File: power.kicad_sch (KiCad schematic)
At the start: 49 parts, among them J1 Battery 1, J7 Battery 2, J8 USB, U1 AMS1117-3.3, U5 TPS56A37RPAR, U6 TPS56A37RPAR

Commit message: Update Cout models for servo motor power and extended pground
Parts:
- C15, C16: footprint Capacitor_SMD:C_0805_2012Metric -> Capacitor_SMD:C_1210_3225Metric
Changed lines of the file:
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@@
 			)
 		)
-		(property "Footprint" "Capacitor_SMD:C_0805_2012Metric"
+		(property "Footprint" "Capacitor_SMD:C_1210_3225Metric"
 			(at 202.8952 40.64 0)
 			(effects
@@
 			)
 		)
-		(property "Datasheet" "~"
+		(property "Datasheet" "HRE CGA1210X6S106K350QT"
 			(at 201.93 36.83 0)
 			(effects
@@
 			)
 		)
-		(property "Footprint" "Capacitor_SMD:C_0805_2012Metric"
+		(property "Footprint" "Capacitor_SMD:C_1210_3225Metric"
 			(at 213.0552 40.64 0)
 			(effects
@@
 			)
 		)
-		(property "Datasheet" "~"
+		(property "Datasheet" "HRE CGA1210X6S106K350QT"
 			(at 212.09 36.83 0)
 			(effects

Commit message: update inductor
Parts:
- L1: footprint Inductor_SMD:L_0805_2012Metric_Pad1.05x1.20mm_HandSolder -> 74438357033:WE-MAPI_4030
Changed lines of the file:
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@@
 			)
 		)
-		(property "Footprint" "Inductor_SMD:L_0805_2012Metric_Pad1.05x1.20mm_HandSolder"
+		(property "Footprint" "74438357033:WE-MAPI_4030"
 			(at 184.15 31.75 0)
 			(effects
@@
 			)
 		)
-		(property "Datasheet" "~"
+		(property "Datasheet" "FTC404030S3R3MGCA"
 			(at 184.15 31.75 0)
 			(effects

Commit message: Sync
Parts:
- removed C18, C19, C38, C39: 10uF, Capacitor_SMD:C_0805_2012Metric, symbol Device:C
- removed C32, C36: 0.1uF, Capacitor_SMD:C_0805_2012Metric, symbol Device:C
- removed C33: 47nF, Capacitor_SMD:C_0805_2012Metric, symbol Device:C
- removed C37: 150pF, Capacitor_SMD:C_0805_2012Metric, symbol Device:C
- removed D4: B540C-13-F, B540C_13_F:DIOM6959X245N, symbol B540C-13-F:B540C-13-F
- removed D7: RED, LED_SMD:LED_0805_2012Metric, symbol Device:LED
- removed F2: C1F-5, C1F_5:FUSC3215X83N, symbol C1F-5:C1F-5
- removed J7: Battery 2, 39-28-1023:CONN_SD-5566-002_02_MOL, symbol 39-28-1023:39281023
- removed L2: 3.3uH, Inductor_SMD:L_0805_2012Metric_Pad1.05x1.20mm_HandSolder, symbol Device:L_Ferrite
- removed R12: 1k5, Resistor_SMD:R_0805_2012Metric_Pad1.20x1.40mm_HandSolder, symbol Device:R
- removed R21: 169kR, Capacitor_SMD:C_0805_2012Metric, symbol Device:R
- removed R22: 36.1kR, Capacitor_SMD:C_0805_2012Metric, symbol Device:R
- removed R23: 52.3kR, Capacitor_SMD:C_0805_2012Metric, symbol Device:R
- removed R24: 10kR, Capacitor_SMD:C_0805_2012Metric, symbol Device:R
- removed R30: 49.9R, Capacitor_SMD:C_0805_2012Metric, symbol Device:R
- removed R31: 73.2kR, Capacitor_SMD:C_0805_2012Metric, symbol Device:R
- removed U6: TPS56A37RPAR, RPA0010A-MFG, symbol TPS56A37RPAR:TPS56A37RPAR
- added C29, C30: 10uF, Capacitor_SMD:C_1206_3216Metric, symbol Device:C
- added C31, C35: 0.1uF, Capacitor_SMD:C_0805_2012Metric, symbol Device:C
- added C34: 47nF, Capacitor_SMD:C_0805_2012Metric, symbol Device:C
- added C40: 150pF, Capacitor_SMD:C_0805_2012Metric, symbol Device:C
- added C41, C42: 10uF, Capacitor_SMD:C_1210_3225Metric, symbol Device:C
- added D6: B540C-13-F, B540C_13_F:DIOM6959X245N, symbol B540C-13-F:B540C-13-F
- added D8: RED, LED_SMD:LED_0805_2012Metric, symbol Device:LED
- added F3: C1F-5, C1F_5:FUSC3215X83N, symbol C1F-5:C1F-5
- added J3: Battery 1, 1724480002:MOLEX_1724480002, symbol 39-28-1023:39281023
- added L3: 3.3uH, 74438357033:WE-MAPI_4030, symbol Device:L_Ferrite
- added R36: 169kR, Capacitor_SMD:C_0805_2012Metric, symbol Device:R
- added R37: 36.1kR, Capacitor_SMD:C_0805_2012Metric, symbol Device:R
- added R38: 52.3kR, Capacitor_SMD:C_0805_2012Metric, symbol Device:R
- added R39: 10kR, Capacitor_SMD:C_0805_2012Metric, symbol Device:R
- added R40: 49.9R, Capacitor_SMD:C_0805_2012Metric, symbol Device:R
- added R41: 73.2kR, Capacitor_SMD:C_0805_2012Metric, symbol Device:R
- added R42: 1k5, Capacitor_SMD:C_0805_2012Metric, symbol Device:R
- added U8: TPS56A37RPAR, RPA0010A-MFG, symbol TPS56A37RPAR:TPS56A37RPAR
- J1: footprint 39-28-1023:CONN_SD-5566-002_02_MOL -> 1724480002:MOLEX_1724480002
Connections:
- net 5V_CAM: now also C41.1, C42.1, L3.2, R40.1, R42.1
- net BT_CAM: now also C35.1, U8.7 (BOOT)
- net EN_CAM_PWR: now also R36.2, R37.1, U8.1 (EN)
- net FB_CAM_PWR: now also C40.2, R39.1, R41.2, U8.2 (FB)
- net GND: now also C29.2, C30.2, C31.2, C34.2, C41.2, C42.2, D8.1 (K), J3.2, R37.2, R38.1, R39.2, U8.3 (AGND), U8.9 (PGND)
- net MODE_CAM: now also R38.2, U8.10 (MODE)
- net SS_CAM: now also C34.1, U8.5 (SS)
- net SW_CAM_PWR: now also C35.2, L3.1, U8.6 (SW)
- net VIN_CAM: now also C29.1, C30.1, C31.1, D6.C, R36.1, U8.8 (VIN)
- new net: C40.1, R40.2, R41.1
- new net: F3.1, J3.1
- new net: D8.2 (A), R42.2
- new net BAT_2: D6.A, F3.2
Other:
- note added: "LED Indicate Battery Supply to Camera"
- note removed: "LED Indicate Battery Supply to Cameras"
- moved on the sheet: C10, C11, C12, C13, C14, C15, C16, C17, C7, C8, D1, D2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

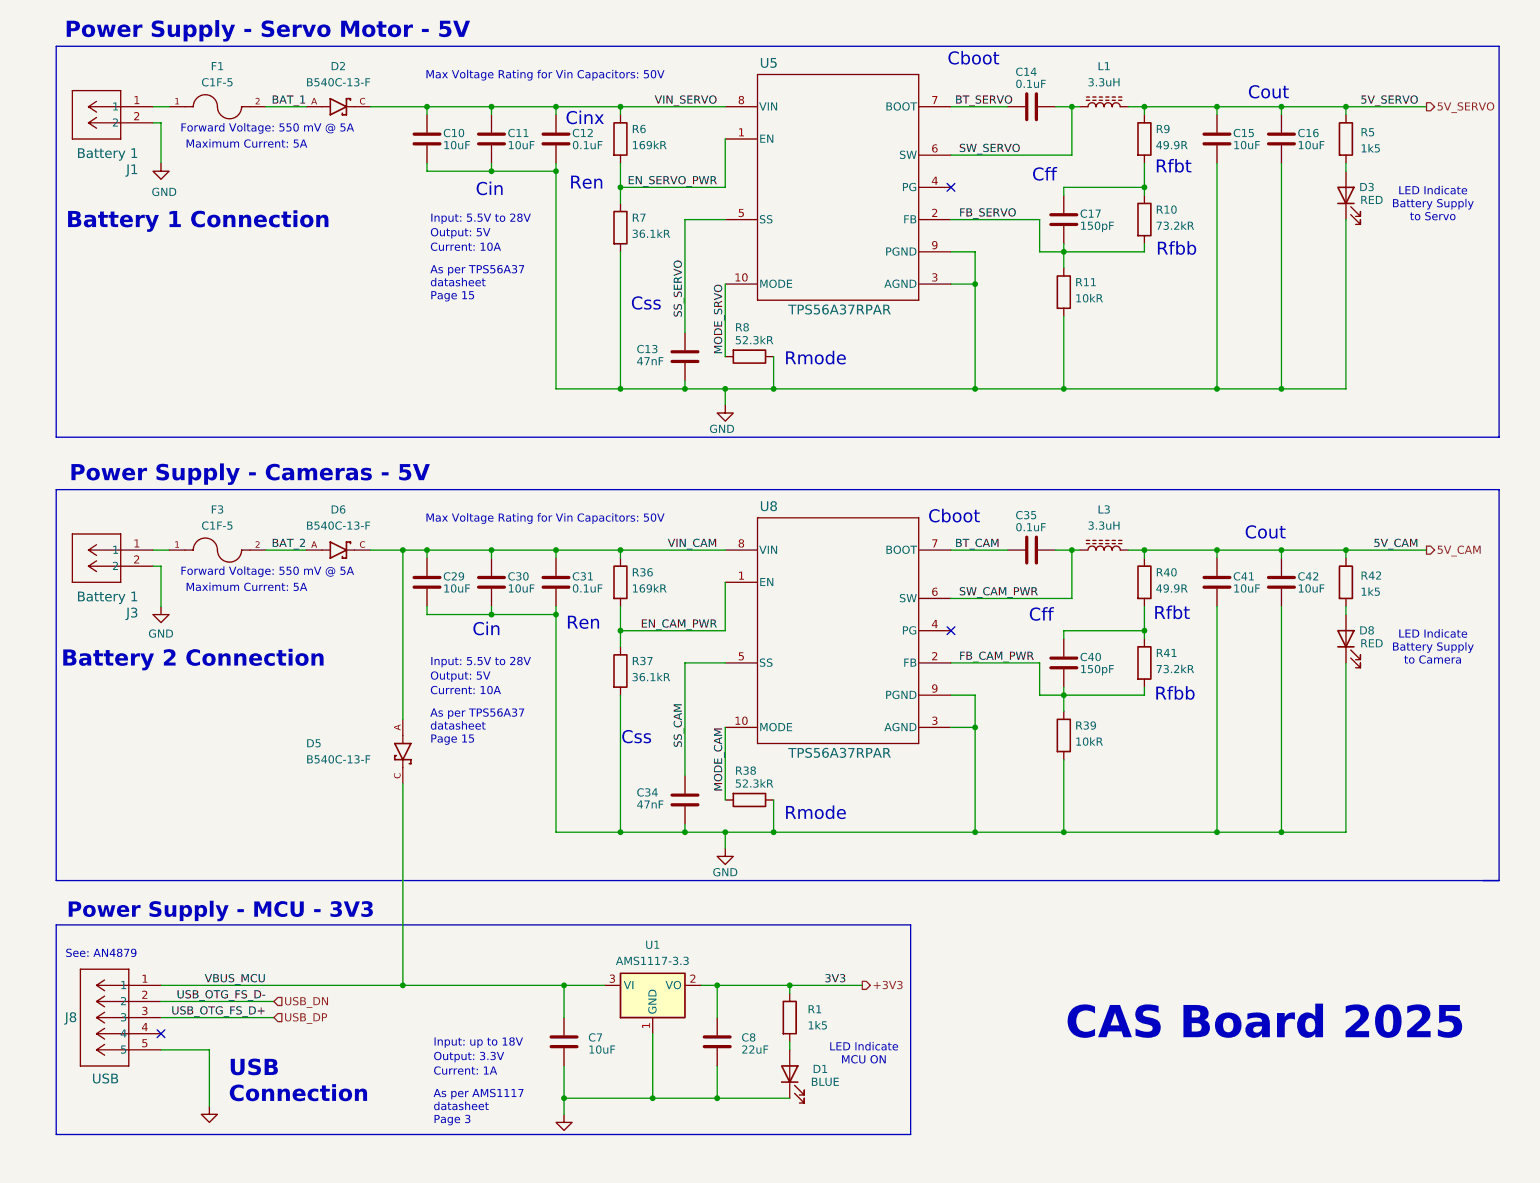
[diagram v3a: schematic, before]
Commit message: Revised to improve buck converters and free up space on board
Fixed overvoltage error on encoder (5v -> 3v)
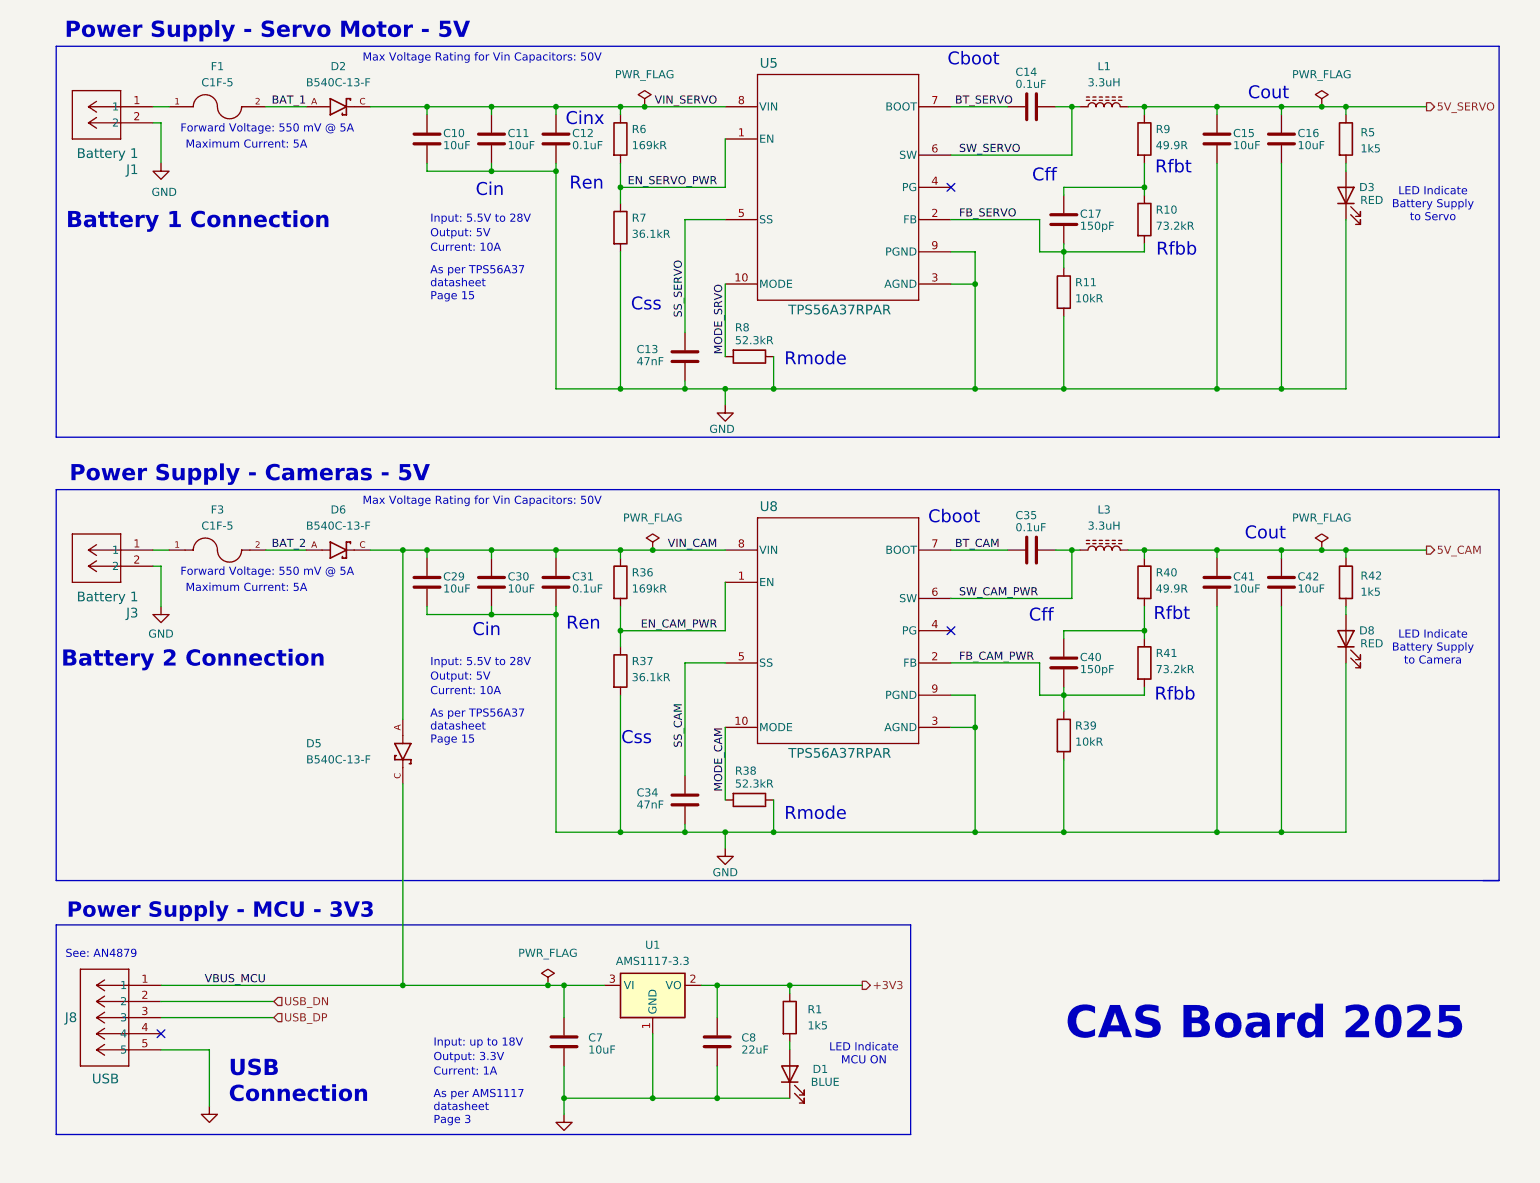
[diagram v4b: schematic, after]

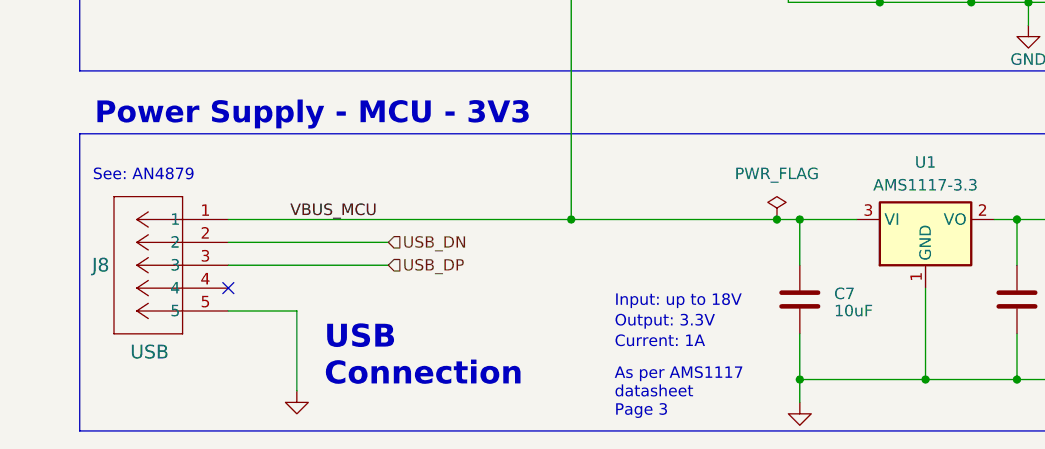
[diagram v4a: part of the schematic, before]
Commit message: Use LCSC parts only
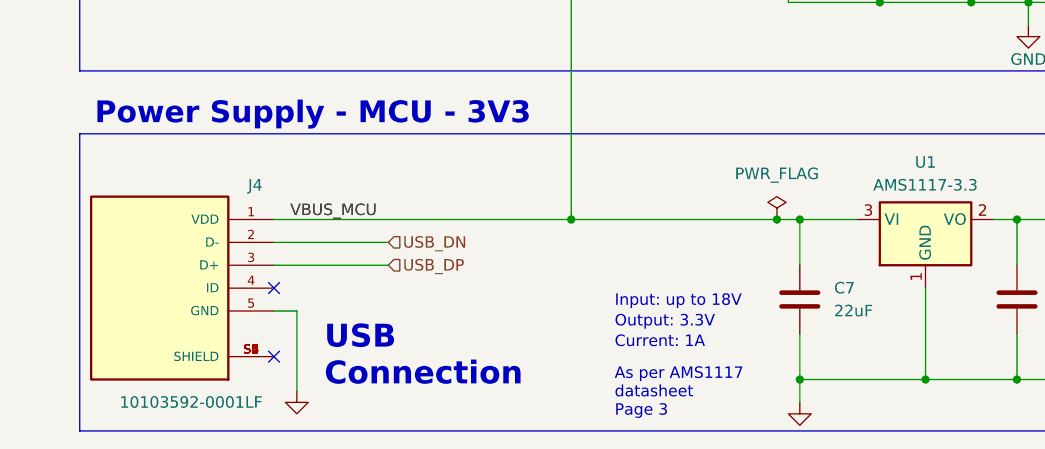
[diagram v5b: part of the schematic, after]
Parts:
- removed J8: USB, KiCADv6:CON00317_5_MOL, symbol 2025-06-16_04-10-11:675031020
- added J4: 10103592-0001LF, USB:AMPHENOL_10103592-0001LF, symbol USB conn:10103592-0001LF
- C7: value 10uF -> 22uF
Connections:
- net GND: now also J4.5 (GND)
- net USB_DN: now also J4.2 (D-)
- net USB_DP: now also J4.3 (D+)
- net VBUS_MCU: now also J4.1 (VDD)
- new net: J4.S1 (SHIELD), J4.S2 (SHIELD), J4.S3 (SHIELD), J4.S4 (SHIELD), J4.S5 (SHIELD), J4.S6 (SHIELD)
- no-connect marks 3 -> 4
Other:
- note removed: "See: AN4879"
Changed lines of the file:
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@@
 		)
 	)
-	(text "See: AN4879\n"
-		(exclude_from_sim no)
-		(at 26.162 162.814 0)
-		(effects
-			(font
-				(size 1.27 1.27)
-			)
-		)
-	)
 	(text "Forward Voltage: 550 mV @ 5A"
 		(exclude_from_sim no)
@@
 	)
 	(no_connect
-		(at 160.02 111.76)
+		(at 40.64 182.88)
 	)
 	(no_connect
-		(at 35.56 175.26)
+		(at 160.02 111.76)
 	)
 	(no_connect
 		(at 160.02 41.91)
 	)
+	(no_connect
+		(at 40.64 175.26)
+	)
 	(wire
 		(pts
@@
 	(wire
 		(pts
-			(xy 35.56 170.18) (xy 53.34 170.18)
+			(xy 40.64 170.18) (xy 53.34 170.18)
 		)
 		(stroke
@@
 	(wire
 		(pts
-			(xy 35.56 167.64) (xy 73.66 167.64)
+			(xy 40.64 167.64) (xy 73.66 167.64)
 		)
 		(stroke
@@
 	(wire
 		(pts
-			(xy 35.56 172.72) (xy 53.34 172.72)
+			(xy 40.64 172.72) (xy 53.34 172.72)
 		)
 		(stroke
@@
 	(wire
 		(pts
-			(xy 35.56 177.8) (xy 43.18 177.8)
+			(xy 40.64 177.8) (xy 43.18 177.8)
 		)
 		(stroke
@@
 	)
 	(symbol
-		(lib_id "Device:LED")
-		(at 134.62 181.61 90)
+		(lib_id "USB conn:10103592-0001LF")
+		(at 27.94 175.26 0)
+		(mirror y)
 		(unit 1)
 		(exclude_from_sim no)
@@
 		(on_board yes)
 		(dnp no)
-		(property "Reference" "D1"
-			(at 139.446 180.848 90)
+		(property "Reference" "J4"
+			(at 39.37 163.83 0)
 			(effects
 				(font
 					(size 1.27 1.27)
 				)
+				(justify left)
 			)
 		)
-		(property "Value" "BLUE"
-			(at 140.208 182.88 90)
+		(property "Value" "10103592-0001LF"
+			(at 39.37 187.96 0)
 			(effects
 				(font
 					(size 1.27 1.27)
 				)
+				(justify left)
 			)
 		)
-		(property "Footprint" "LED_SMD:LED_0805_2012Metric"
-			(at 134.62 181.61 0)
+		(property "Footprint" "USB:AMPHENOL_10103592-0001LF"
+			(at 27.94 175.26 0)
+			(effects
+				(font
+					(size 1.27 1.27)
+				)
+				(justify bottom)
+				(hide yes)
+			)
+		)
+		(property "Datasheet" ""
+			(at 27.94 175.26 0)
 			(effects
 				(font
@@
 			)
 		)
-		(property "Datasheet" "~"
-			(at 134.62 181.61 0)
+		(property "Description" ""
+			(at 27.94 175.26 0)
 			(effects
 				(font
@@
 			)
 		)
-		(property "Description" "Light emitting diode"
-			(at 134.62 181.61 0)
+		(property "MF" "Amphenol"
+			(at 27.94 175.26 0)
 			(effects
 				(font
 					(size 1.27 1.27)
 				)
+				(justify bottom)
 				(hide yes)
 			)
 		)
-		(property "Sim.Pins" "1=K 2=A"
-			(at 134.62 181.61 0)
+		(property "MAXIMUM_PACKAGE_HEIGHT" "3.25mm"
+			(at 27.94 175.26 0)
 			(effects
 				(font
 					(size 1.27 1.27)
 				)
+				(justify bottom)
 				(hide yes)
 			)
 		)
-		(pin "1"
+		(property "Package" "None"
+			(at 27.94 175.26 0)
+			(effects
+				(font
+					(size 1.27 1.27)
+				)
+				(justify bottom)
+				(hide yes)
+			)
+		)
+		(property "Price" "None"
+			(at 27.94 175.26 0)
+			(effects
+				(font
+					(size 1.27 1.27)
+				)
+				(justify bottom)
+				(hide yes)
+			)
+		)
+		(property "Check_prices" "https://www.snapeda.com/parts/10103592-0001LF/Amphenol/view-part/?ref=eda"
+			(at 27.94 175.26 0)
+			(effects
+				(font
+					(size 1.27 1.27)
+				)
+				(justify bottom)
+				(hide yes)
+			)
+		)
+		(property "STANDARD" "Manufacturer Recommendations"
+			(at 27.94 175.26 0)
+			(effects
+				(font
+					(size 1.27 1.27)
+				)
+				(justify bottom)
+				(hide yes)
+			)
+		)
+		(property "PARTREV" "B"
+			(at 27.94 175.26 0)
+			(effects
+				(font
+					(size 1.27 1.27)
+				)
+				(justify bottom)
+				(hide yes)
+			)
+		)
+		(property "SnapEDA_Link" "https://www.snapeda.com/parts/10103592-0001LF/Amphenol/view-part/?ref=snap"
+			(at 27.94 175.26 0)
+			(effects
+				(font
+					(size 1.27 1.27)
+				)
+				(justify bottom)
+				(hide yes)
+			)
+		)
+		(property "MP" "10103592-0001LF"
+			(at 27.94 175.26 0)
+			(effects
+				(font
+					(size 1.27 1.27)
+				)
+				(justify bottom)
+				(hide yes)
+			)
+		)
+		(property "Description_1" "Conn;Data;USB;TypeB;Reverse;5Cnts;RightAngle;Micro;SMT | Amphenol FCI (Amphenol CS) 10103592-0001LF"
+			(at 27.94 175.26 0)
+			(effects
+				(font
+					(size 1.27 1.27)
+				)
+				(justify bottom)
+				(hide yes)
+			)
+		)
+		(property "MANUFACTURER" "Amphenol"
+			(at 27.94 175.26 0)
+			(effects
+				(font
+					(size 1.27 1.27)
+				)
+				(justify bottom)
+				(hide yes)
+			)
+		)
+		(property "Availability" "In Stock"
+			(at 27.94 175.26 0)
+			(effects
+				(font
+					(size 1.27 1.27)
+				)
+				(justify bottom)
+				(hide yes)
+			)
+		)
+		(property "SNAPEDA_PN" "10103592-0001LF"
+			(at 27.94 175.26 0)
+			(effects
+				(font
+					(size 1.27 1.27)
+				)
+				(justify bottom)
+				(hide yes)
+			)
+		)
+		(pin "S2"
+		)
+		(pin "S1"
+		)
+		(pin "S6"
+		)
+		(pin "3"
+		)
+		(pin "S5"
+		)
+		(pin "S4"
+		)
+		(pin "4"
 		)
 		(pin "2"
 		)
+		(pin "1"
+		)
+		(pin "5"
+		)
+		(pin "S3"
+		)
 		(instances
-			(project "SimplerFlight_v2"
+			(project ""
 				(path "/05521696-5bcb-4d0e-9e87-bbc993e58ce4/9c9f06bc-de18-4b20-a7a6-016e96dea1cf"
-					(reference "D1")
+					(reference "J4")
 					(unit 1)
 				)
@@
 	)
 	(symbol
-		(lib_id "2025-06-16_04-10-11:675031020")
-		(at 25.4 172.72 0)
-		(mirror y)
+		(lib_id "Device:LED")
+		(at 134.62 181.61 90)
 		(unit 1)
 		(exclude_from_sim no)
@@
 		(on_board yes)
 		(dnp no)
-		(property "Reference" "J8"
-			(at 22.352 172.72 0)
+		(property "Reference" "D1"
+			(at 139.446 180.848 90)
 			(effects
 				(font
-					(size 1.524 1.524)
+					(size 1.27 1.27)
 				)
-				(justify left)
 			)
 		)
-		(property "Value" "USB"
-			(at 28.956 182.372 0)
+		(property "Value" "BLUE"
+			(at 140.208 182.88 90)
 			(effects
 				(font
-					(size 1.524 1.524)
+					(size 1.27 1.27)
 				)
-				(justify left)
 			)
 		)
-		(property "Footprint" "KiCADv6:CON00317_5_MOL"
-			(at 25.4 172.72 0)
+		(property "Footprint" "LED_SMD:LED_0805_2012Metric"
+			(at 134.62 181.61 0)
 			(effects
 				(font
 					(size 1.27 1.27)
-					(italic yes)
 				)
 				(hide yes)
 			)
 		)
-		(property "Datasheet" "675031020"
-			(at 25.4 172.72 0)
+		(property "Datasheet" "~"
+			(at 134.62 181.61 0)
 			(effects
 				(font
 					(size 1.27 1.27)
-					(italic yes)
 				)
 				(hide yes)
 			)
 		)
-		(property "Description" ""
-			(at 25.4 172.72 0)
+		(property "Description" "Light emitting diode"
+			(at 134.62 181.61 0)
 			(effects
 				(font
@@
 			)
 		)
-		(pin "4"
-		)
-		(pin "3"
+		(property "Sim.Pins" "1=K 2=A"
+			(at 134.62 181.61 0)
+			(effects
+				(font
+					(size 1.27 1.27)
+				)
+				(hide yes)
+			)
 		)
 		(pin "1"
 		)
-		(pin "5"
-		)
 		(pin "2"
 		)
@@
 			(project "SimplerFlight_v2"
 				(path "/05521696-5bcb-4d0e-9e87-bbc993e58ce4/9c9f06bc-de18-4b20-a7a6-016e96dea1cf"
-					(reference "J8")
+					(reference "D1")
 					(unit 1)
 				)
@@
 		(fields_autoplaced yes)
 		(property "Reference" "C7"
-			(at 102.87 175.8949 0)
+			(at 102.87 175.2599 0)
 			(effects
 				(font
@@
 			)
 		)
-		(property "Value" "10uF"
-			(at 102.87 177.8 0)
+		(property "Value" "22uF"
+			(at 102.87 177.7999 0)
 			(effects
 				(font
